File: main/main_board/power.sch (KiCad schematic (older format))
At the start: 46 parts, among them J1 Power, U3 MCP1755S-3302E/DB, U4 MCP1755S-3302E/DB, U7 MCP1755S-5002E/DB

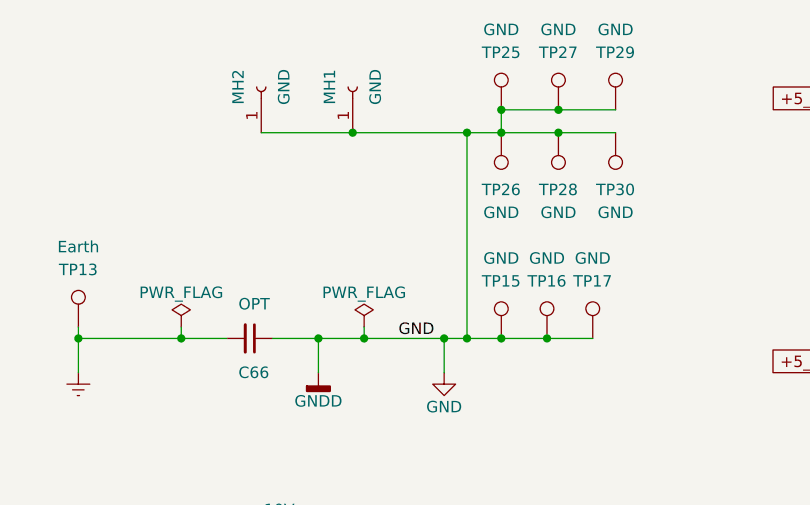
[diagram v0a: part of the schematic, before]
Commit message: Main board seems to be about ready to be set off. Added gerber files. Made new footprints for the LEDs and DAC, since nothing in the standard footprints was a good match for the manufacturer recommended pattern. Moved around component values on the fab layer. Tweaked ground plane thermal via and fill width so that we get continuity between pins on the PCIe connectors. Moved OVDD vias to also avoid ground plane slotting. Added local copper pours on planes on U6 thermal pad to prevent thermal reliefs on the thermal vias.
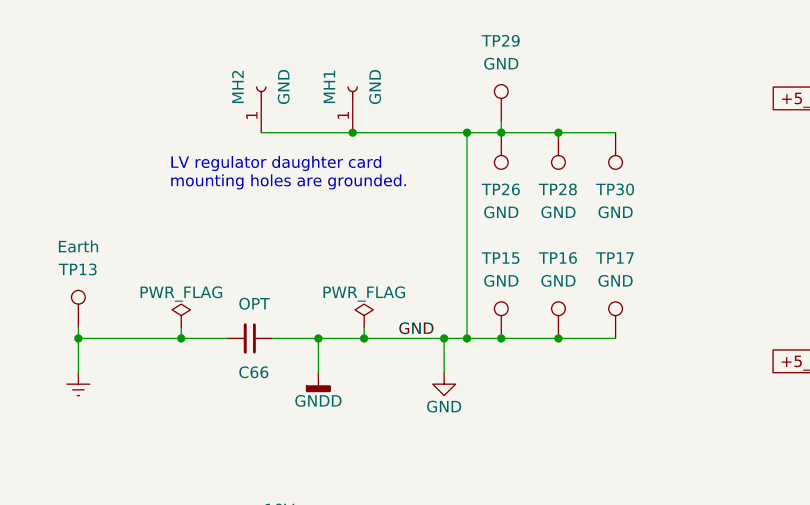
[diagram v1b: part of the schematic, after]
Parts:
- removed TP25, TP27: GND, TestPoint:TestPoint_Keystone_5000-5004_Miniature, symbol Connector:TestPoint
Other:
- note added: "LV regulator daughter card\nmounting holes are grounded."
- moved on the sheet: TP16, TP17, TP29
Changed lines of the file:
@@
 AR Path="/5E62FD57/5E630FEC/5F142D31" Ref="TP?"  Part="1"
 AR Path="/5E525FC9/5F142D31" Ref="TP15"  Part="1"
-F 0 "TP15" H 5450 2500 50  0000 C CNN
-F 1 "GND" H 5450 2600 50  0000 C CNN
+F 0 "TP15" H 5450 2600 50  0000 C CNN
+F 1 "GND" H 5450 2500 50  0000 C CNN
 F 2 "input:TestPoint_THTPad_D5.0mm_Drill2.41mm" H 5650 2250 50  0001 C CNN
 F 3 "~" H 5650 2250 50  0001 C CNN
@@
 L Connector:TestPoint TP?
 U 1 1 5F147AB3
-P 5650 2250
+P 5700 2250
 AR Path="/5DFCF14D/5DA78AA2/5F147AB3" Ref="TP?"  Part="1"
 AR Path="/5DFCF14D/5E295469/5F147AB3" Ref="TP?"  Part="1"
@@
 AR Path="/5E62FD57/5E630FEC/5F147AB3" Ref="TP?"  Part="1"
 AR Path="/5E525FC9/5F147AB3" Ref="TP16"  Part="1"
-F 0 "TP16" H 5650 2500 50  0000 C CNN
-F 1 "GND" H 5650 2600 50  0000 C CNN
-F 2 "input:TestPoint_THTPad_D5.0mm_Drill2.41mm" H 5850 2250 50  0001 C CNN
-F 3 "~" H 5850 2250 50  0001 C CNN
-F 4 "39" H 5650 2250 50  0001 C CNN "DK line"
-F 5 "TERM TURRET HOLLOW L=6.75MM TIN" H 5650 2250 50  0001 C CNN "Description"
-F 6 "36-1540-2-ND" H 5650 2250 50  0001 C CNN "Digikey"
-F 7 "1540-2" H 5650 2250 50  0001 C CNN "MPN"
-F 8 "Keystone Electronics" H 5650 2250 50  0001 C CNN "Manufacturer"
-	1    5650 2250
+F 0 "TP16" H 5700 2600 50  0000 C CNN
+F 1 "GND" H 5700 2500 50  0000 C CNN
+F 2 "input:TestPoint_THTPad_D5.0mm_Drill2.41mm" H 5900 2250 50  0001 C CNN
+F 3 "~" H 5900 2250 50  0001 C CNN
+F 4 "39" H 5700 2250 50  0001 C CNN "DK line"
+F 5 "TERM TURRET HOLLOW L=6.75MM TIN" H 5700 2250 50  0001 C CNN "Description"
+F 6 "36-1540-2-ND" H 5700 2250 50  0001 C CNN "Digikey"
+F 7 "1540-2" H 5700 2250 50  0001 C CNN "MPN"
+F 8 "Keystone Electronics" H 5700 2250 50  0001 C CNN "Manufacturer"
+	1    5700 2250
 	1    0    0    -1
 $EndComp
@@
 L Connector:TestPoint TP?
 U 1 1 5F147D04
-P 5850 2250
+P 5950 2250
 AR Path="/5DFCF14D/5DA78AA2/5F147D04" Ref="TP?"  Part="1"
 AR Path="/5DFCF14D/5E295469/5F147D04" Ref="TP?"  Part="1"
@@
 AR Path="/5E62FD57/5E630FEC/5F147D04" Ref="TP?"  Part="1"
 AR Path="/5E525FC9/5F147D04" Ref="TP17"  Part="1"
-F 0 "TP17" H 5850 2500 50  0000 C CNN
-F 1 "GND" H 5850 2600 50  0000 C CNN
-F 2 "input:TestPoint_THTPad_D5.0mm_Drill2.41mm" H 6050 2250 50  0001 C CNN
-F 3 "~" H 6050 2250 50  0001 C CNN
-F 4 "39" H 5850 2250 50  0001 C CNN "DK line"
-F 5 "TERM TURRET HOLLOW L=6.75MM TIN" H 5850 2250 50  0001 C CNN "Description"
-F 6 "36-1540-2-ND" H 5850 2250 50  0001 C CNN "Digikey"
-F 7 "1540-2" H 5850 2250 50  0001 C CNN "MPN"
-F 8 "Keystone Electronics" H 5850 2250 50  0001 C CNN "Manufacturer"
-	1    5850 2250
-	1    0    0    -1
-$EndComp
-Wire Wire Line
-	5450 2250 5650 2250
+F 0 "TP17" H 5950 2600 50  0000 C CNN
+F 1 "GND" H 5950 2500 50  0000 C CNN
+F 2 "input:TestPoint_THTPad_D5.0mm_Drill2.41mm" H 6150 2250 50  0001 C CNN
+F 3 "~" H 6150 2250 50  0001 C CNN
+F 4 "39" H 5950 2250 50  0001 C CNN "DK line"
+F 5 "TERM TURRET HOLLOW L=6.75MM TIN" H 5950 2250 50  0001 C CNN "Description"
+F 6 "36-1540-2-ND" H 5950 2250 50  0001 C CNN "Digikey"
+F 7 "1540-2" H 5950 2250 50  0001 C CNN "MPN"
+F 8 "Keystone Electronics" H 5950 2250 50  0001 C CNN "Manufacturer"
+	1    5950 2250
+	1    0    0    -1
+$EndComp
+Wire Wire Line
+	5450 2250 5700 2250
 Connection ~ 5450 2250
-Connection ~ 5650 2250
-Wire Wire Line
-	5650 2250 5850 2250
+Connection ~ 5700 2250
+Wire Wire Line
+	5700 2250 5950 2250
 $Comp
 L Connector:TestPoint TP?
@@
 $Comp
 L Connector:TestPoint TP?
-U 1 1 5F1F37D8
-P 5450 1250
-AR Path="/5DFCF14D/5DA78AA2/5F1F37D8" Ref="TP?"  Part="1"
-AR Path="/5DFCF14D/5E295469/5F1F37D8" Ref="TP?"  Part="1"
-AR Path="/5DFCF14D/5E195558/5F1F37D8" Ref="TP?"  Part="1"
-AR Path="/5F1F37D8" Ref="TP?"  Part="1"
-AR Path="/5E525FC9/5F1F37D8" Ref="TP25"  Part="1"
-F 0 "TP25" H 5450 1500 50  0000 C CNN
-F 1 "GND" H 5450 1600 50  0000 C CNN
-F 2 "TestPoint:TestPoint_Keystone_5000-5004_Miniature" H 5650 1250 50  0001 C CNN
-F 3 "~" H 5650 1250 50  0001 C CNN
-F 4 "Do Not Populate" H 5450 1250 50  0001 C CNN "Description"
-F 5 "DNP" H 5450 1250 50  0001 C CNN "MPN"
-	1    5450 1250
-	1    0    0    -1
-$EndComp
-$Comp
-L Connector:TestPoint TP?
-U 1 1 5F1F3E71
-P 5700 1250
-AR Path="/5DFCF14D/5DA78AA2/5F1F3E71" Ref="TP?"  Part="1"
-AR Path="/5DFCF14D/5E295469/5F1F3E71" Ref="TP?"  Part="1"
-AR Path="/5DFCF14D/5E195558/5F1F3E71" Ref="TP?"  Part="1"
-AR Path="/5F1F3E71" Ref="TP?"  Part="1"
-AR Path="/5E525FC9/5F1F3E71" Ref="TP27"  Part="1"
-F 0 "TP27" H 5700 1500 50  0000 C CNN
-F 1 "GND" H 5700 1600 50  0000 C CNN
-F 2 "TestPoint:TestPoint_Keystone_5000-5004_Miniature" H 5900 1250 50  0001 C CNN
-F 3 "~" H 5900 1250 50  0001 C CNN
-F 4 "Do Not Populate" H 5700 1250 50  0001 C CNN "Description"
-F 5 "DNP" H 5700 1250 50  0001 C CNN "MPN"
-	1    5700 1250
-	1    0    0    -1
-$EndComp
-$Comp
-L Connector:TestPoint TP?
 U 1 1 5F1F4086
-P 5950 1250
+P 5450 1300
 AR Path="/5DFCF14D/5DA78AA2/5F1F4086" Ref="TP?"  Part="1"
 AR Path="/5DFCF14D/5E295469/5F1F4086" Ref="TP?"  Part="1"
@@
 AR Path="/5F1F4086" Ref="TP?"  Part="1"
 AR Path="/5E525FC9/5F1F4086" Ref="TP29"  Part="1"
-F 0 "TP29" H 5950 1500 50  0000 C CNN
-F 1 "GND" H 5950 1600 50  0000 C CNN
-F 2 "TestPoint:TestPoint_Keystone_5000-5004_Miniature" H 6150 1250 50  0001 C CNN
-F 3 "~" H 6150 1250 50  0001 C CNN
-F 4 "Do Not Populate" H 5950 1250 50  0001 C CNN "Description"
-F 5 "DNP" H 5950 1250 50  0001 C CNN "MPN"
-	1    5950 1250
+F 0 "TP29" H 5450 1650 50  0000 C CNN
+F 1 "GND" H 5450 1550 50  0000 C CNN
+F 2 "TestPoint:TestPoint_Keystone_5000-5004_Miniature" H 5650 1300 50  0001 C CNN
+F 3 "~" H 5650 1300 50  0001 C CNN
+F 4 "Do Not Populate" H 5450 1300 50  0001 C CNN "Description"
+F 5 "DNP" H 5450 1300 50  0001 C CNN "MPN"
+	1    5450 1300
 	1    0    0    -1
 $EndComp
@@
 Connection ~ 5700 1350
 Wire Wire Line
-	5950 1250 5700 1250
-Wire Wire Line
-	5700 1250 5450 1250
-Connection ~ 5700 1250
-Wire Wire Line
-	5450 1250 5450 1350
-Connection ~ 5450 1250
+	5450 1300 5450 1350
 Connection ~ 5450 1350
 Wire Wire Line
@@
 Connection ~ 4800 1350
 Connection ~ 5300 1350
+Text Notes 4000 1600 0    50   ~ 0
+LV regulator daughter card\nmounting holes are grounded.
 $EndSCHEMATC
